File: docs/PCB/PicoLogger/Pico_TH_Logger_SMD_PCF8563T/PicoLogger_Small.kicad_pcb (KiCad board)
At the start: 2 copper layers, 51.5 x 83 mm, 27 parts, among them J1 Sensor, J2 LCD 16x2, J3 Additional connector, J5 SPI, SW1 SW_Push, SW2 SW_Push, U1 PCF8563T, Y1 Crystal

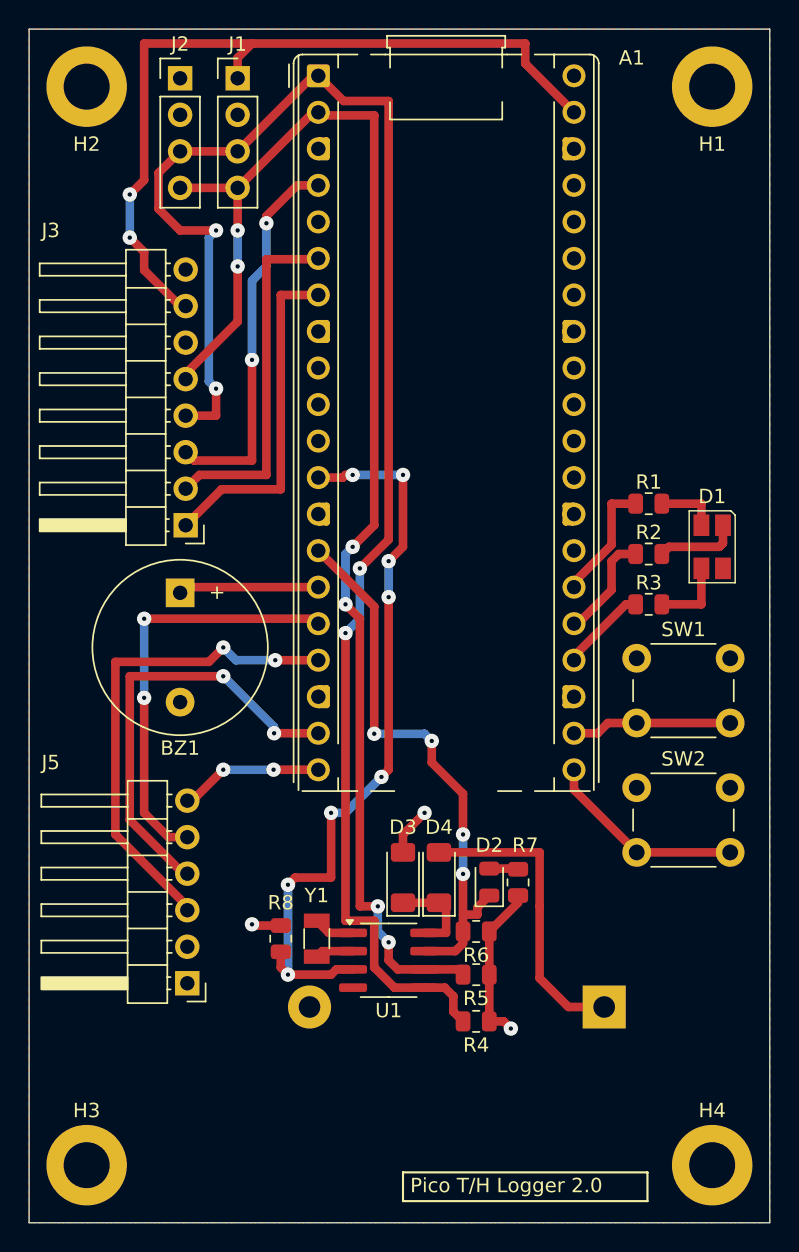
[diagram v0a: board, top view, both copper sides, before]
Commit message: Logger docs updated.
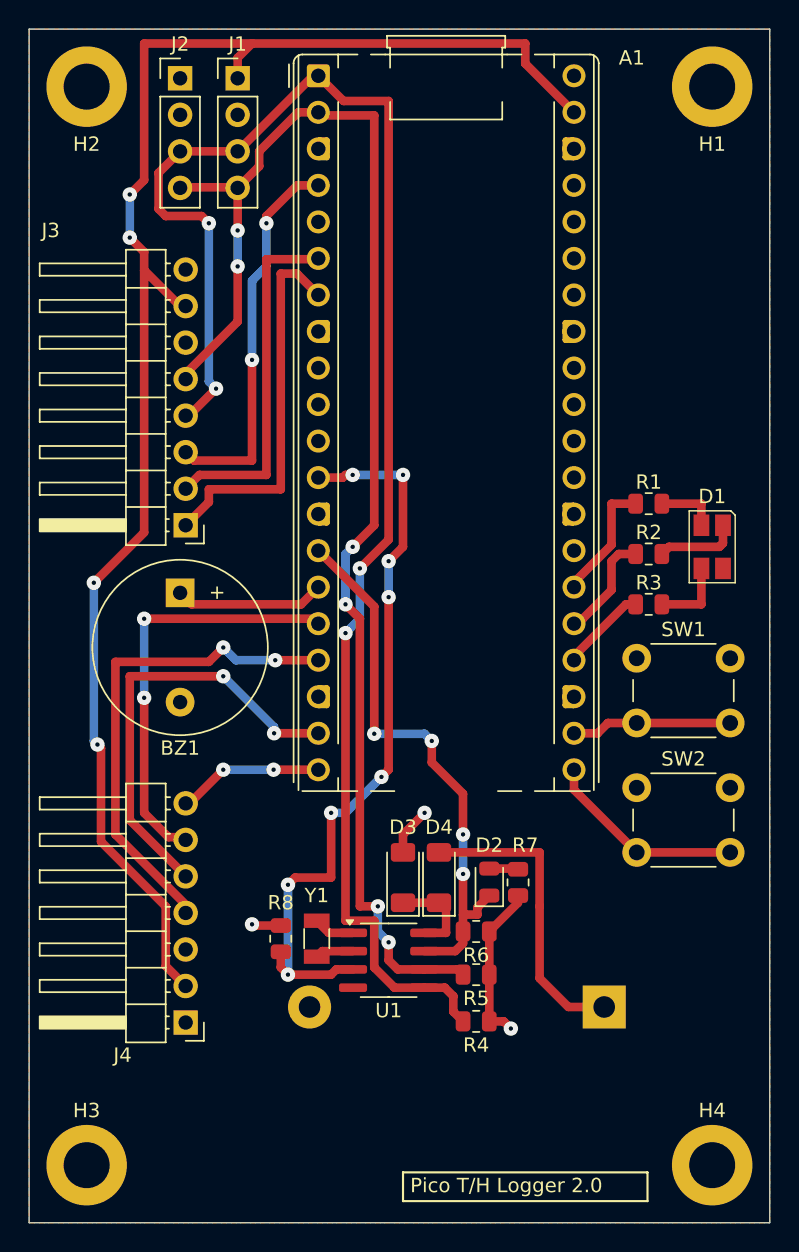
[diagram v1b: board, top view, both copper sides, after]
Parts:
- removed J5: SPI, Connector_PinHeader_2.54mm:PinHeader_1x06_P2.54mm_Horizontal
- added J4: SPI, Connector_PinHeader_2.54mm:PinHeader_1x07_P2.54mm_Horizontal, F.Cu at (145.4, 104.1)
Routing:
- net +3.3V: track 55.6 -> 109.5 mm, vias 2 -> 4
- net RX: track 23.8 -> 26.4 mm
- net SDA: track 114.5 -> 113.0 mm
- net GPIO11: track 9.77 -> 10.4 mm
- net SCL: track 97.9 -> 98.5 mm

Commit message: Loggers corrected based on JLCPCB DFM check.
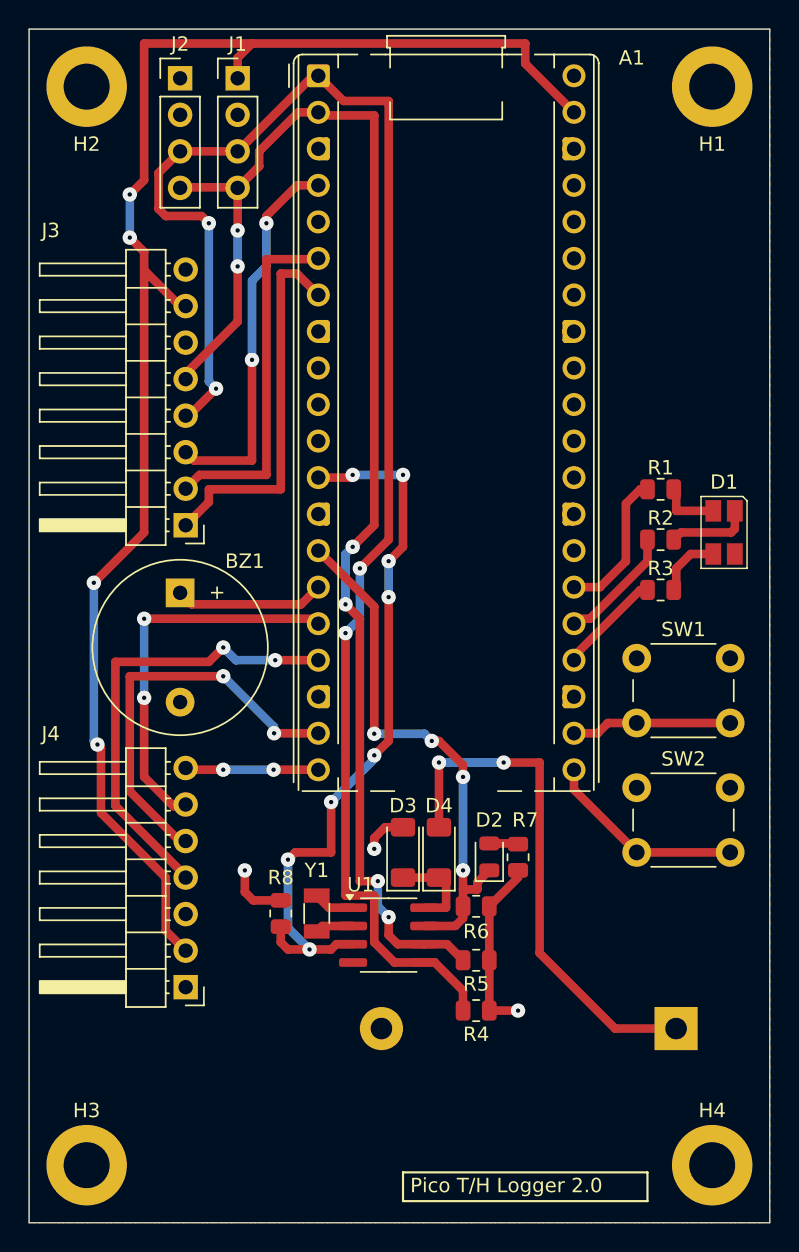
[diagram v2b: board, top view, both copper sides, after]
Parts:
- moved BT1 5.22 mm to (179.5, 104.5)
- moved J4 2.46 mm to (145.4, 101.6)
- moved D2 1.75 mm to (166.5, 92.6)
- moved D3 1.75 mm to (160.5, 92.2)
- moved D4 1.75 mm to (163.0, 92.2)
- moved R6 1.75 mm to (165.6, 96.0)
- moved R7 1.75 mm to (168.5, 92.6)
- moved R8 1.75 mm to (152.0, 96.5)
- moved U1 1.75 mm to (159.5, 98.0)
- moved Y1 1.75 mm to (154.5, 96.5)
- moved D1 1.30 mm to (182.8, 70.0)
- moved R1 1.30 mm to (178.4, 67.0)
- moved R2 1.30 mm to (178.4, 70.5)
- moved R3 1.30 mm to (178.4, 74.0)
- moved R5 1.00 mm to (165.6, 99.8)
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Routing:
- net +BATT: track 21.4 -> 36.8 mm, vias 0 -> 2
- net +5V: track 16.7 -> 19.9 mm
- net +3.3V: track 109.5 -> 107.1 mm
- net SPI RX: track 29.5 -> 27.1 mm
- net SDA: track 113.0 -> 110.9 mm
- net SPI CSn: track 34.2 -> 32.1 mm
- net SPI SCK: track 30.5 -> 28.5 mm
- net GPIO9: track 52.6 -> 50.8 mm
- net GPIO20: track 8.56 -> 10.3 mm
- net GPIO10: track 39.1 -> 37.7 mm
- net SCL: track 98.5 -> 97.1 mm
- net GPIO19: track 6.98 -> 8.41 mm
- net GPIO18: track 6.06 -> 7.29 mm
- net SPI TX: track 10.5 -> 9.64 mm
- net Net-(D1-VDD): track 5.25 -> 4.56 mm

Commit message: Updated docs.
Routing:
- net RX: track 26.4 -> 22.6 mm
- net +3.3V: track 107.1 -> 105.7 mm
- net TX: track 24.6 -> 23.5 mm
- net SDA: track 110.9 -> 109.8 mm
- net Net-(D1-DI): track 4.15 -> 3.37 mm
- net SPI SCK: track 28.5 -> 27.9 mm
- net SPI CSn: track 32.1 -> 31.5 mm
